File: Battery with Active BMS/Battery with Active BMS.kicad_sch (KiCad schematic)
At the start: 62 parts, among them J1 Balancer Connector, J2 74651195R, J3 74651195R, Q1 IRFP7430PBF, Q2 IRFP7430PBF, U1 TLI4971A050T5UE0001XUMA1, U3 MCP3008, U4 TC4427CPA, U5 LM2574HVN-5

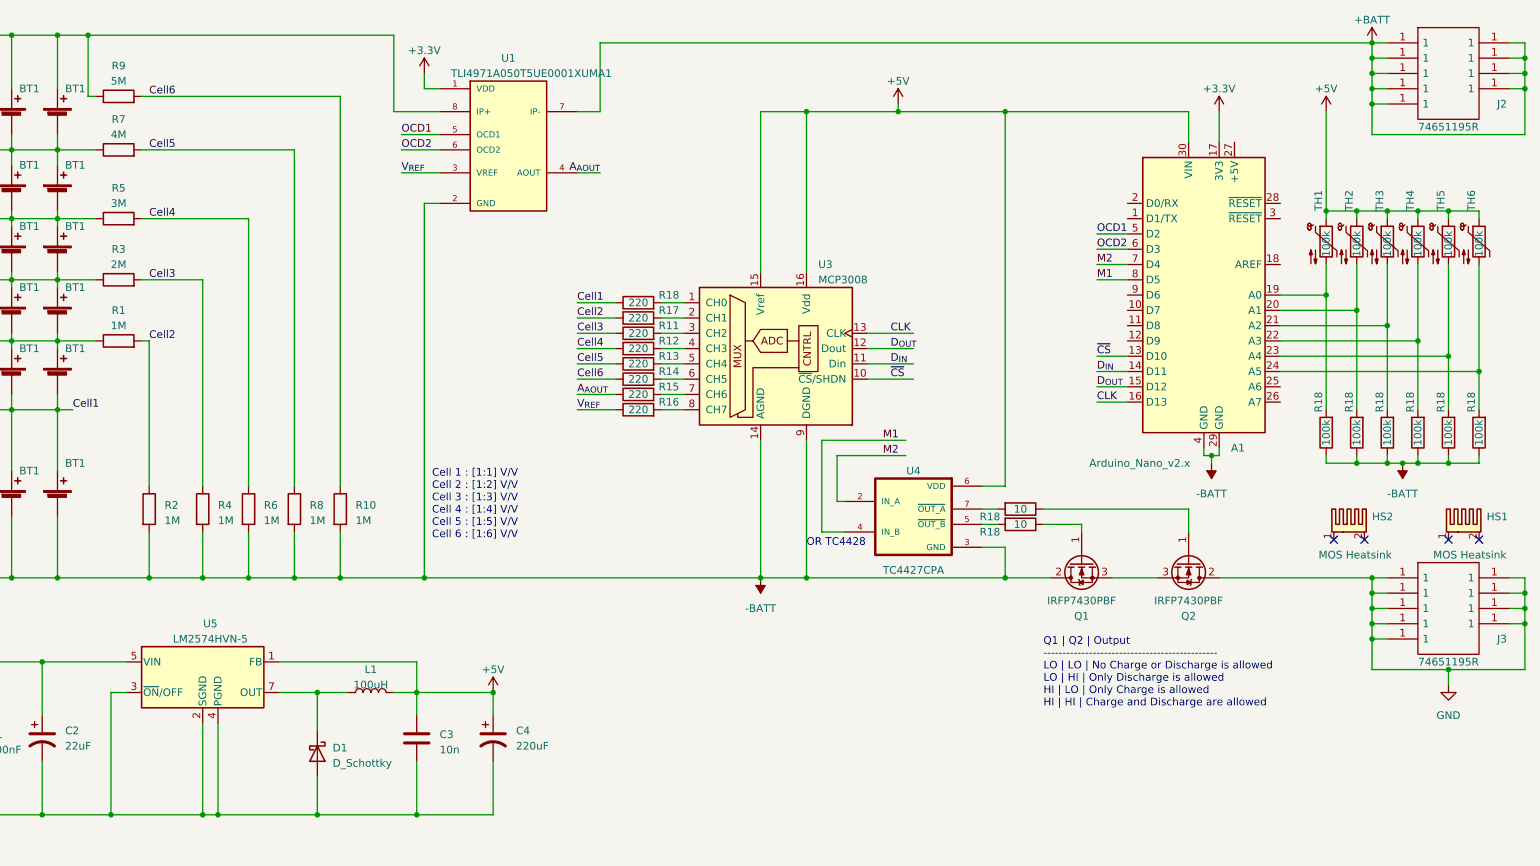
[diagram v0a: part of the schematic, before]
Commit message: Updated Active BMS and BOM
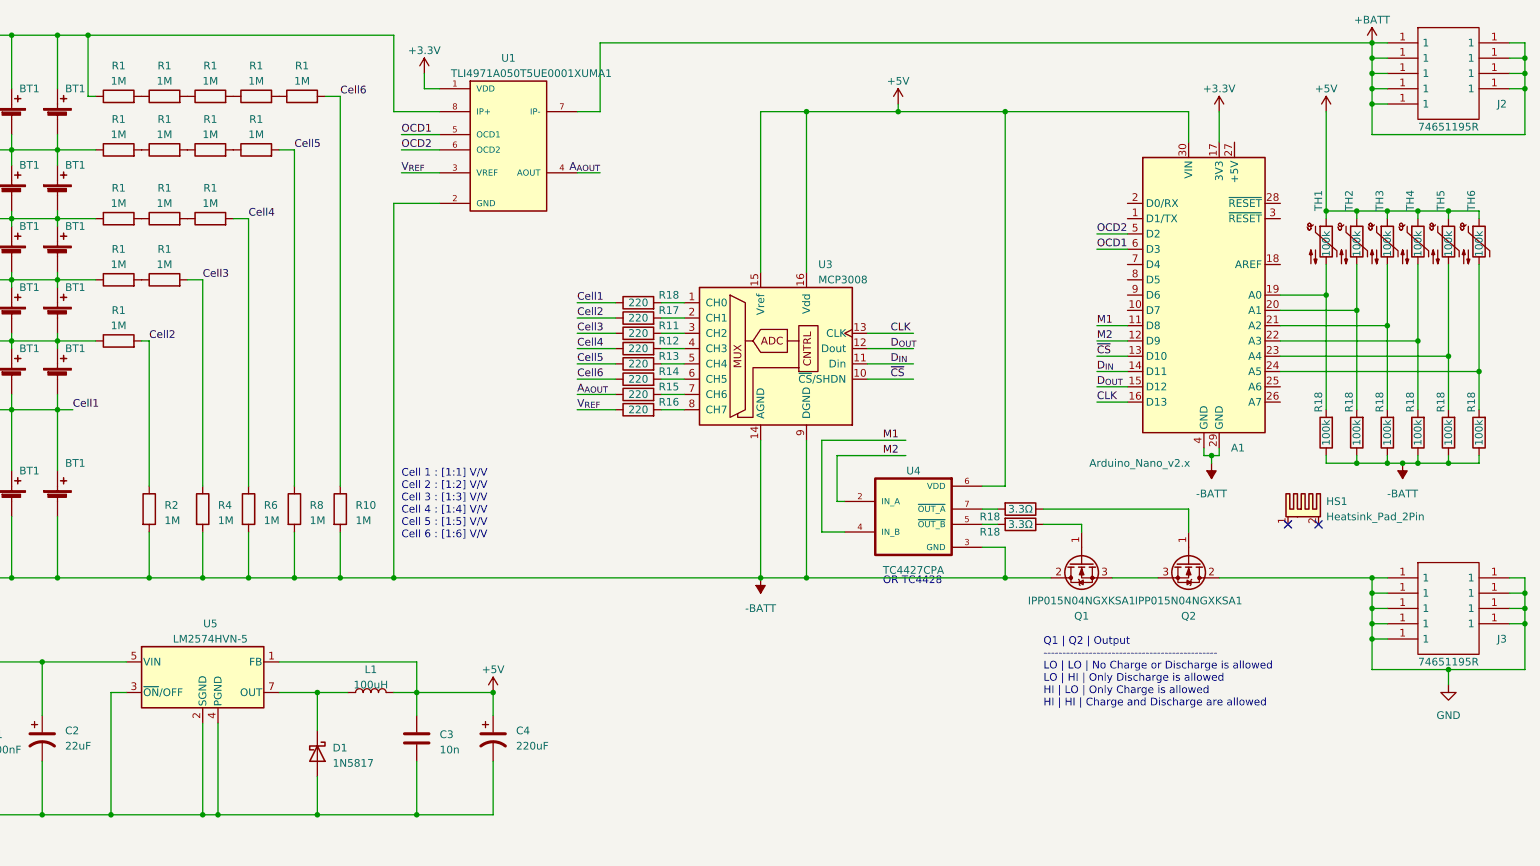
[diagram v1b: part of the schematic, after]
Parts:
- removed HS2: MOS Heatsink, Heatsink:Heatsink_Fischer_FK224xx2201_25x8.3mm, symbol Mechanical:Heatsink_Pad_2Pin
- removed R3: 2M, Resistor_SMD:R_0805_2012Metric_Pad1.20x1.40mm_HandSolder, symbol Device:R
- removed R5: 3M, Resistor_SMD:R_0805_2012Metric_Pad1.20x1.40mm_HandSolder, symbol Device:R
- removed R7: 4M, Resistor_SMD:R_0805_2012Metric_Pad1.20x1.40mm_HandSolder, symbol Device:R
- removed R9: 5M, Resistor_SMD:R_0805_2012Metric_Pad1.20x1.40mm_HandSolder, symbol Device:R
- added R1 (x14): 1M, Resistor_THT:R_Axial_DIN0207_L6.3mm_D2.5mm_P10.16mm_Horizontal, symbol Device:R
- C1: Part (none) -> 08055C104KAT2A
- C2: Part (none) -> EEEFK1V220R
- C3: footprint Capacitor_SMD:C_0805_2012Metric_Pad1.18x1.45mm_HandSolder -> Capacitor_SMD:C_1206_3216Metric_Pad1.33x1.80mm_HandSolder; Part (none) -> CC1206KRX7R9103
- D1: value D_Schottky -> 1N5817
- HS1: value MOS Heatsink -> Heatsink_Pad_2Pin; footprint Heatsink:Heatsink_Fischer_FK224xx2201_25x8.3mm -> Heatsink:Heatsink_Fischer_SK104-STC-STIC_35x13mm_2xDrill2.5mm
- J1: footprint Connector_PinSocket_2.54mm:PinSocket_1x07_P2.54mm_Vertical -> Connector_JST:JST_EH_B7B-EH-A_1x07_P2.50mm_Vertical
- Q1, Q2: value IRFP7430PBF -> IPP015N04NGXKSA1; footprint Package_TO_SOT_THT:TO-247-3_Vertical -> Package_TO_SOT_THT:TO-220F-3_Vertical
- R1, R10, R2, R4, R6, R8: footprint Resistor_SMD:R_0805_2012Metric_Pad1.20x1.40mm_HandSolder -> Resistor_THT:R_Axial_DIN0207_L6.3mm_D2.5mm_P10.16mm_Horizontal
- R18: value 10 -> 3.3Ω
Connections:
- net Cell3: now also R1.2
- net Cell4: now also R1.2
- net Cell5: now also R1.2
- net Cell6: now also R1.2
- net M1: now also A1.11 (D8); no longer A1.8 (D5)
- net M2: now also A1.12 (D9); no longer A1.7 (D4)
- net OCD1: now also A1.6 (D3); no longer A1.5 (D2)
- net OCD2: now also A1.5 (D2); no longer A1.6 (D3)
- net at BT1.1 (+), BT1.1 (+), J1.1 (Pin_1)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: now also R1.1
- net at BT1.1 (+), BT1.1 (+), BT1.2 (-)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: now also R1.1 (x3)
- new net: R1.1, R1.2 (x10)
- no-connect marks 4 -> 2

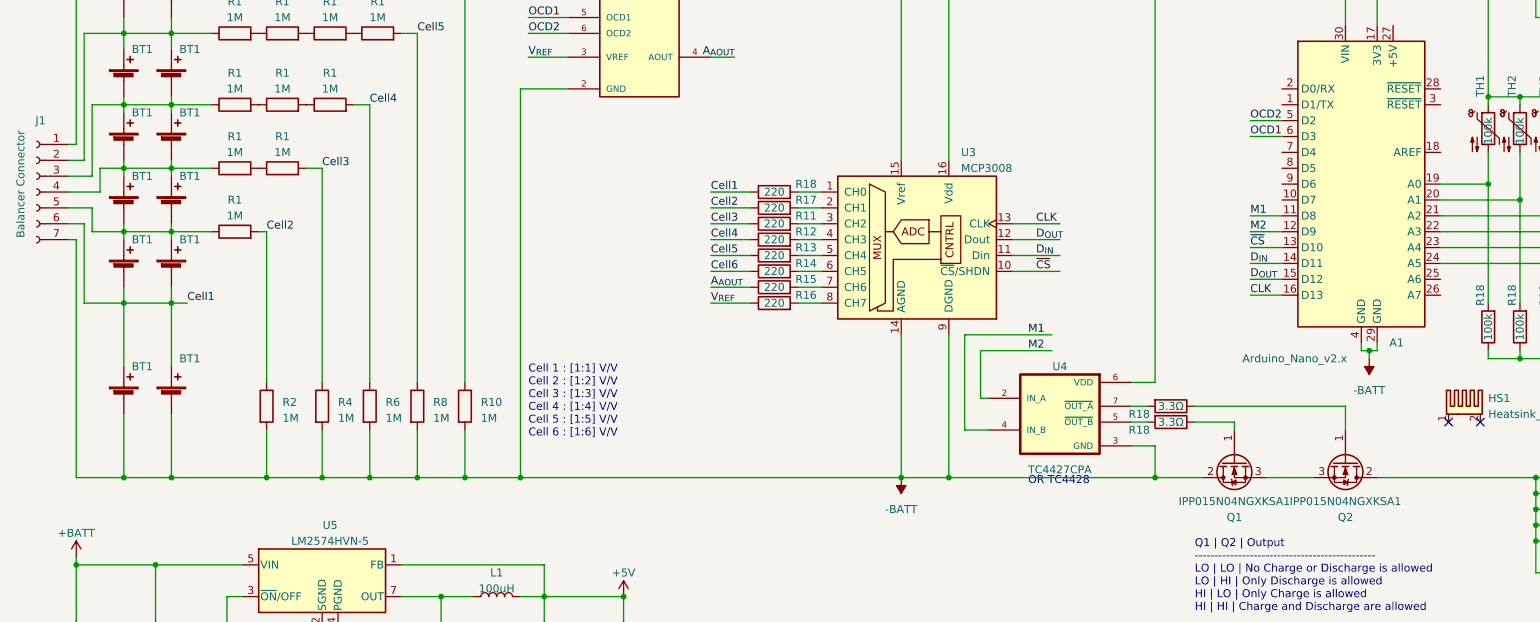
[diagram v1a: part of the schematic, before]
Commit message: Updated Battery with Active BMS Schem&PCB&BOM
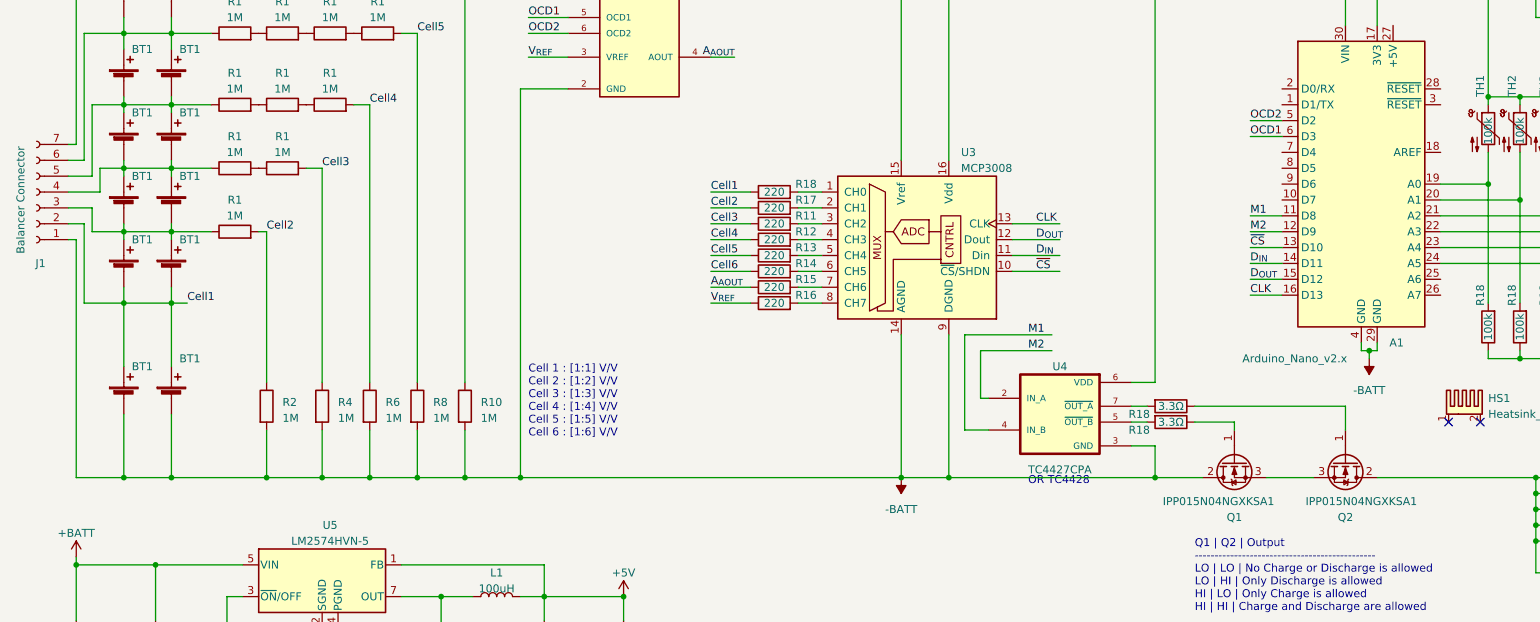
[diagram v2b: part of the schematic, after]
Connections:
- net -BATT: now also J1.1 (Pin_1); no longer J1.7 (Pin_7)
- net Cell1: now also J1.2 (Pin_2); no longer J1.6 (Pin_6)
- net at BT1.1 (+), BT1.1 (+), R1.1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: now also J1.7 (Pin_7); no longer J1.1 (Pin_1)
- net at BT1.1 (+), BT1.1 (+), BT1.2 (-)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: now also J1.6 (Pin_6); no longer J1.2 (Pin_2)
- net at BT1.1 (+), BT1.1 (+), BT1.2 (-)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: now also J1.5 (Pin_5); no longer J1.3 (Pin_3)
- net at BT1.1 (+), BT1.1 (+), BT1.2 (-)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: now also J1.3 (Pin_3); no longer J1.5 (Pin_5)
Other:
- moved on the sheet: J1
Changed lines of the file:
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@@
     )
   )
-  (symbol (lib_id "Connector:Conn_01x07_Socket") (at 16.51 60.96 0) (mirror y) (unit 1)
-    (in_bom yes) (on_board yes) (dnp no)
-    (property "Reference" "J1" (at 17.145 49.53 0)
-      (effects (font (size 1.27 1.27)))
-    )
-    (property "Value" "Balancer Connector" (at 13.97 59.69 90)
+  (symbol (lib_id "Connector:Conn_01x07_Socket") (at 16.51 60.96 180) (unit 1)
+    (in_bom yes) (on_board yes) (dnp no)
+    (property "Reference" "J1" (at 17.145 72.39 0)
+      (effects (font (size 1.27 1.27)))
+    )
+    (property "Value" "Balancer Connector" (at 13.97 62.23 90)
       (effects (font (size 1.27 1.27)))
     )
@@
       (effects (font (size 1.27 1.27)))
     )
-    (property "Value" "IPP015N04NGXKSA1" (at 226.06 110.49 90)
+    (property "Value" "IPP015N04NGXKSA1" (at 228.6 110.49 90)
       (effects (font (size 1.27 1.27)))
     )
@@
       (effects (font (size 1.27 1.27)))
     )
-    (property "Value" "IPP015N04NGXKSA1" (at 208.28 110.49 90)
-      (effects (font (size 1.27 1.27)))
-    )
+    (property "Value" "IPP015N04NGXKSA1" (at 205.74 110.49 90)
+      (effects (font (size 1.27 1.27)))
+    )

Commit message: Motor Driver V1.0
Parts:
- removed A1: Arduino_Nano_v2.x, Module:Arduino_Nano_WithMountingHoles, symbol MCU_Module:Arduino_Nano_v2.x
- removed BT1 (x12): Battery_Cell, Battery:BatteryHolder_MPD_BH-18650-PC2, symbol Device:Battery_Cell
- removed C1: 100nF, Capacitor_SMD:C_0805_2012Metric_Pad1.18x1.45mm_HandSolder, symbol Device:C
- removed C2: 22uF, Capacitor_SMD:CP_Elec_5x5.8, symbol Device:C_Polarized_US
- removed C3: 10n, Capacitor_SMD:C_1206_3216Metric_Pad1.33x1.80mm_HandSolder, symbol Device:C
- removed C4: 220uF, Capacitor_SMD:CP_Elec_6.3x5.8, symbol Device:C_Polarized_US
- removed D1: 1N5817, Diode_THT:D_DO-15_P5.08mm_Vertical_KathodeUp, symbol Device:D_Schottky
- removed HS1: Heatsink_Pad_2Pin, Heatsink:Heatsink_Fischer_SK104-STC-STIC_35x13mm_2xDrill2.5mm, symbol Mechanical:Heatsink_Pad_2Pin
- removed J1: Balancer Connector, Connector_JST:JST_EH_B7B-EH-A_1x07_P2.50mm_Vertical, symbol Connector:Conn_01x07_Socket
- removed J2, J3: 74651195R, TerminalBlock_Wuerth:Wuerth_REDCUBE-THR_WP-THRSH_74651195_THR, symbol 74651195R:74651195R
- removed L1: 100uH, Inductor_THT:L_Radial_D10.5mm_P5.00mm_Abacron_AISR-01, symbol Device:L
- removed Q1, Q2: IPP015N04NGXKSA1, Package_TO_SOT_THT:TO-220F-3_Vertical, symbol Device:Q_NMOS_GDS
- removed R1 (x15), R2: 1M, Resistor_THT:R_Axial_DIN0207_L6.3mm_D2.5mm_P10.16mm_Horizontal, symbol Device:R
- removed R12, R16, R17, R18: 220, Resistor_SMD:R_0805_2012Metric_Pad1.20x1.40mm_HandSolder, symbol Device:R
- removed R18 (x6): 100k, Resistor_SMD:R_0805_2012Metric_Pad1.20x1.40mm_HandSolder, symbol Device:R
- removed R18 (x2): 3.3Ω, Resistor_SMD:R_0805_2012Metric_Pad1.20x1.40mm_HandSolder, symbol Device:R
- removed TH1, TH2, TH3, TH4, TH5, TH6: 100k, Connector_PinSocket_2.54mm:PinSocket_1x02_P2.54mm_Vertical, symbol Device:Thermistor_NTC
- removed U1: TLI4971A050T5UE0001XUMA1, Package_SON:Infineon_PG-TISON-8-5, symbol TLI4971A050T5UE0001XUMA1:TLI4971A050T5UE0001XUMA1
- removed U3: MCP3008, Package_DIP:DIP-16_W7.62mm_LongPads, symbol Analog_ADC:MCP3008
- removed U4: TC4427CPA, Package_DIP:DIP-8_W7.62mm_LongPads, symbol TC4427CPA:TC4427CPA
- removed U5: LM2574HVN-5, Package_DIP:DIP-8_W7.62mm, symbol Regulator_Switching:LM2574HVN-5
- added B1, B2, B3, B4, B5, B6: 7461383, lib:M5 Screw Terminal, symbol Battery with Active BMS-altium-import:root_0_Screw Terminal
- added BT1, BT10, BT11, BT12, BT13, BT14, BT15, BT16, BT17, BT18, BT2, BT3, BT4, BT5, BT6, BT7, BT8, BT9: Battery_Cell, lib:21700, symbol Device:Battery_Cell
- added C1, C2, C3, C4, C5: Capacitor, Capacitor_SMD:C_0805_2012Metric_Pad1.18x1.45mm_HandSolder, symbol Battery with Active BMS-altium-import:root_0_Capacitor-Symbol-1
- added H1, H2, H3, H4: MountingHole_Pad, MountingHole:MountingHole_5.3mm_M5_Pad_Via, symbol Mechanical:MountingHole_Pad
- added H10, H11, H12, H5, H6, H7, H8, H9: MountingHole, MountingHole:MountingHole_2.5mm_Pad, symbol Mechanical:MountingHole
- added J1: B7B-EH-A(LF)(SN), Connector_JST:JST_EH_B7B-EH-A_1x07_P2.50mm_Vertical, symbol Battery with Active BMS-altium-import:root_0_5bcee6b94e1fee4be3f4cc3a650a442
- added J2, J3: B7B-EH-A(LF)(SN), Connector_JST:JST_EH_B6B-EH-A_1x06_P2.50mm_Vertical, symbol Battery with Active BMS-altium-import:root_0_5bcee6b94e1fee4be3f4cc3a650a442
- added P1, P5: 22-28-4033, Connector_PinHeader_2.54mm:PinHeader_2x02_P2.54mm_Vertical, symbol Battery with Active BMS-altium-import:root_2_CN-1P-M-R3
- added P2: 61300511121, Connector_PinHeader_2.54mm:PinHeader_2x05_P2.54mm_Vertical, symbol Battery with Active BMS-altium-import:root_2_mirrored_WE-CN-1P-M-R5
- added P3: 61300811121, Connector_PinHeader_2.54mm:PinHeader_2x09_P2.54mm_Vertical, symbol Battery with Active BMS-altium-import:root_0_WE-CN-1P-M-R8
- added Q1, Q2: NMOS, lib:IAUA250N04S6N005AUMA1, symbol Simulation_SPICE:NMOS
- added R1, R12, R16, R17, R18, R19, R2, R20, R21, R24: Res2, Resistor_SMD:R_0805_2012Metric_Pad1.20x1.40mm_HandSolder, symbol Battery with Active BMS-altium-import:root_0_Res2
- added R22, R23, R25, R3, R30, R31, R32, R33, R34, R41, R42, R43, R44, R47, R48, R49, R5, R7, R9: 1M, Resistor_THT:R_Axial_DIN0207_L6.3mm_D2.5mm_P10.16mm_Horizontal, symbol Device:R
- added R26, R27: Res2, Resistor_THT:R_Axial_DIN0207_L6.3mm_D2.5mm_P10.16mm_Horizontal, symbol Battery with Active BMS-altium-import:root_1_Res2
- added R28, R29: Res2, Resistor_SMD:R_0805_2012Metric_Pad1.20x1.40mm_HandSolder, symbol Battery with Active BMS-altium-import:root_1_Res2
- added U1: TLI4971, Package_SON:Infineon_PG-TISON-8-5, symbol Battery with Active BMS-altium-import:root_0_TLI4971
- added U2: ARDUINO_PRO_MINI, lib:MODULE_ARDUINO_PRO_MINI, symbol Battery with Active BMS-altium-import:root_0_ARDUINO_PRO_MINI
- added U3: MPC3008, Package_DIP:DIP-16_W7.62mm, symbol Battery with Active BMS-altium-import:root_0_MPC3008
- added U4: TC4428CPA, Package_DIP:DIP-8_W7.62mm, symbol Battery with Active BMS-altium-import:root_3_IN-MOSDRV-TC1428CPA-8
- added U5: LM78M05CT/NOPB, Connector_PinSocket_2.54mm:PinSocket_1x03_P2.54mm_Vertical, symbol Battery with Active BMS-altium-import:root_0_PM-REG-LM2940-SIL3
- R11, R13, R14, R15: value 220 -> 1M; footprint Resistor_SMD:R_0805_2012Metric_Pad1.20x1.40mm_HandSolder -> Resistor_THT:R_Axial_DIN0207_L6.3mm_D2.5mm_P10.16mm_Horizontal
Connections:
- net +3.3V: now also C3.1, P2.1, R1.2, R2.2, U1.1 (VDD), U2.JP1_4 (VCC), U2.JP6_4 (VCC_1), U3.15 (VREF), U3.16 (VDD), U4.6 (VDD), U5.3 (OUT)
- net CLK: now also U2.JP6_9 (SCK), U3.13 (CLK)
- net Cell1: now also R4.2, R24.1, R3.2
- net Cell2: now also R6.1, R21.1, R43.2
- net Cell3: now also R14.2, R20.1, R44.2; no longer R11.1, R4.1
- net Cell4: now also R13.1, R19.1, R47.2; no longer R6.1
- net Cell5: now also R18.1, R42.1, R48.2; no longer R13.1, R8.1
- net Cell6: now also R17.1, R41.1, R49.2; no longer R10.1, R14.1
- net GND: now also R4.1, B6.1, C1.2, C2.2, C3.2, C4.2, C5.2, P1.2, P1.4, P2.10, P2.2, P2.4, P2.6, P2.8, P3.10, P3.12, P3.14, P3.16, P3.18, P3.2, P3.4, P3.6, P3.8, P5.2, P5.4, Q1.1 (D), R26.1, R27.1, R43.1, R44.1, R47.1, R48.1, R49.1, U1.2 (GND), U2.JP1_5 (GND), U2.JP1_6 (GND), U2.JP6_2 (GND_1), U2.JP7_9 (GND_2), U3.14 (AGND), U3.9 (DGND), U4.3 (GND), U5.2 (GND)
- net OCD1: now also C2.1, P5.1, R1.1, U1.5 (OCD1)
- net OCD2: now also C1.1, P5.3, R2.1, U1.6 (OCD2)
- net ~{CS}: now also U2.JP6_12 (D10), U3.10 (\~{C}S)
- net at R15.2: now also J2.2
- net at R11.2: now also R10.1
- net at R13.2: now also R11.1
- removed net -BATT: R10.2, R4.2, R6.2, R8.2
- net A_{AOUT}: no longer names the net of R15.1
- net A_{AOUT}: now also R22.2
- new net: R7.1, R8.2
- new net: J2.4, R7.2
- new net: R31.1, R32.2
- new net: R30.1, R31.2
- new net: BT1.1 (+), BT2.1 (+), BT3.1 (+), BT4.2 (-), BT5.2 (-), BT6.2 (-), J1.6, J3.6
- new net: B3.1, BT1.2 (-), BT2.2 (-), BT3.2 (-), J1.7
- new net: BT10.2 (-), BT11.2 (-), BT12.2 (-), BT7.1 (+), BT8.1 (+), BT9.1 (+), J1.4, J3.4
- new net: BT4.1 (+), BT5.1 (+), BT6.1 (+), BT7.2 (-), BT8.2 (-), BT9.2 (-), J1.5, J3.5
- new net: B5.1, Q2.1 (D)
- new net: Q2.2 (G), R29.1
- new net: Q1.3 (S), Q2.3 (S)
- new net: B4.1, U1.7 (IP-)
- new net: Q1.2 (G), R28.1
- new net: R28.2, U4.5 (OUTB)
- new net: B2.1, BT16.1 (+), BT17.1 (+), BT18.1 (+), J1.1, J3.1
- new net: R22.1, R23.2
- new net: R12.2, U3.1 (CH0)
- new net: R16.2, U3.2 (CH1)
- new net: R17.2, U3.3 (CH2)
- new net: R18.2, U3.4 (CH3)
- new net: R19.2, U3.5 (CH4)
- new net: R20.2, U3.6 (CH5)
- new net: R21.2, U3.7 (CH6)
- new net: R24.2, U3.8 (CH7)
- new net: R34.1, R41.2
- new net: R33.1, R34.2
- new net: R5.1, R6.2
- new net: J2.5, R5.2
- new net: J2.1, R30.2
- new net: J2.3, R9.2
- new net: J2.6, R3.1
- new net: R32.1, R33.2
- new net: BT13.1 (+), BT14.1 (+), BT15.1 (+), BT16.2 (-), BT17.2 (-), BT18.2 (-), J1.2, J3.2
- new net: BT10.1 (+), BT11.1 (+), BT12.1 (+), BT13.2 (-), BT14.2 (-), BT15.2 (-), J1.3, J3.3
- new net: R14.1, R8.1
- new net: R26.2, U2.JP7_1 (D9), U4.4 (INB)
- new net: R10.2, R9.1
- new net: R29.2, U4.7 (~{OUTA})
- new net: P3.11, U2.JP7_6 (D4)
- new net: P3.13, U2.JP7_5 (D5)
- new net: P3.15, U2.JP7_4 (D6)
- new net: P3.17, U2.JP7_3 (D7)
- new net: P3.7, U2.JP7_8 (D2)
- new net: P3.9, U2.JP7_7 (D3)
- new net: P1.3, U2.JP3_1 (A6)
- new net: R27.2, U2.JP7_2 (D8), U4.2 (INA)
- new net: R25.1, R42.2
- new net: R23.1, R25.2
- new net A0: U2.JP6_8 (A0)
- new net A1: U2.JP6_7 (A1)
- new net A2: U2.JP6_6 (A2)
- new net A3: U2.JP6_5 (A3)
- new net A4: U2.JP2_1 (A4)
- new net A5: U2.JP2_2 (A5)
- new net A7: P1.1, U2.JP3_2 (A7)
- new net AOUT: C5.1, R12.1, U1.4 (Aout)
- new net Batt+: B1.1, U1.8 (IP+), U5.1 (IN)
- new net Copper Conn 1: H1.1, H2.1
- new net Copper Conn 2: H3.1, H4.1
- new net DIN: U2.JP6_11 (MOSI), U3.11 (DIN)
- new net DOUT: U2.JP6_10 (MISO), U3.12 (DOUT)
- new net DTR: U2.JP1_1 (DTR)
- new net DTR_{ISO}: P2.7
- new net RST: P3.1, U2.JP6_3 (RST_1), U2.JP7_10 (RST_2)
- new net RST_{ISO}: P2.9
- new net RX_2: P3.5, U2.JP7_11 (RXI_2)
- new net RX_{0}: U2.JP1_3 (RXI)
- new net RX_{ISO}: P2.3
- new net TX_2: P3.3, U2.JP7_12 (TXO_2)
- new net TX_{0}: U2.JP1_2 (TXO)
- new net TX_{ISO}: P2.5
- new net VREF: C4.1, R16.1, U1.3 (Vref)
- no-connect marks 2 -> 0
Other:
- added sheet Isolator2 (Isolator.kicad_sch)
- added sheet ThermistorLayout (ThermistorLayout.kicad_sch)
- note added: "3.3V Power Rail"
- note added: "Analog Fanout"
- note added: "Copper Connectors"
- note added: "Digital Fanout"
- note added: "HIGH CURRENT"
- note added: "Isolated Programming Terminal"
- note added: "Isolator"
- note added: "Mounting"
- note added: "Signal Filtering"
- note removed: "Cell 1 : [1:1] V/V Cell 2 : [1:2] V/V Cell 3 : [1:3] V/V Cell 4 : [1:4] V/V Cell 5 : [1:5] V/V Cell 6 : [1:6] V/V"
- note removed: "OR TC4428"
- note removed: "Q1 | Q2 | Output ---------------------------------------------- LO | LO | No Charge or Discharge is allowed LO | HI | Only Discharge is allowed HI | LO | Only Charge is allowed HI | HI | Charge and Discharge are allowed"
